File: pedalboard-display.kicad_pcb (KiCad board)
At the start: 2 copper layers, 174 x 111 mm, 206 parts, among them J1 Conn_01x03_Pin, J2 Conn_01x03_Pin, J3 OLED

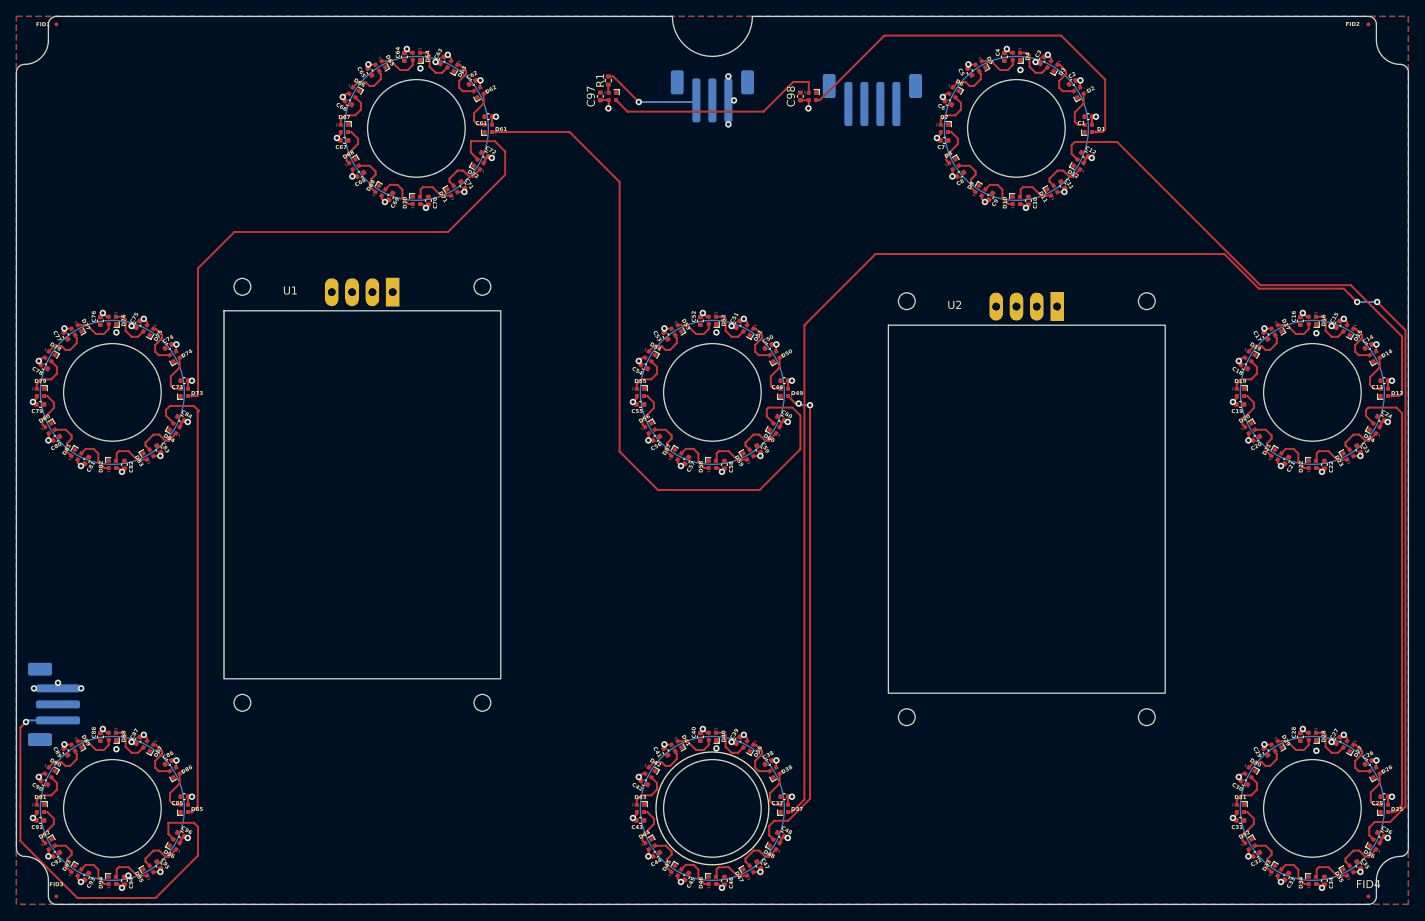
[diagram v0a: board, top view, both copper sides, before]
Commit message: Add 3d models for JST connectors
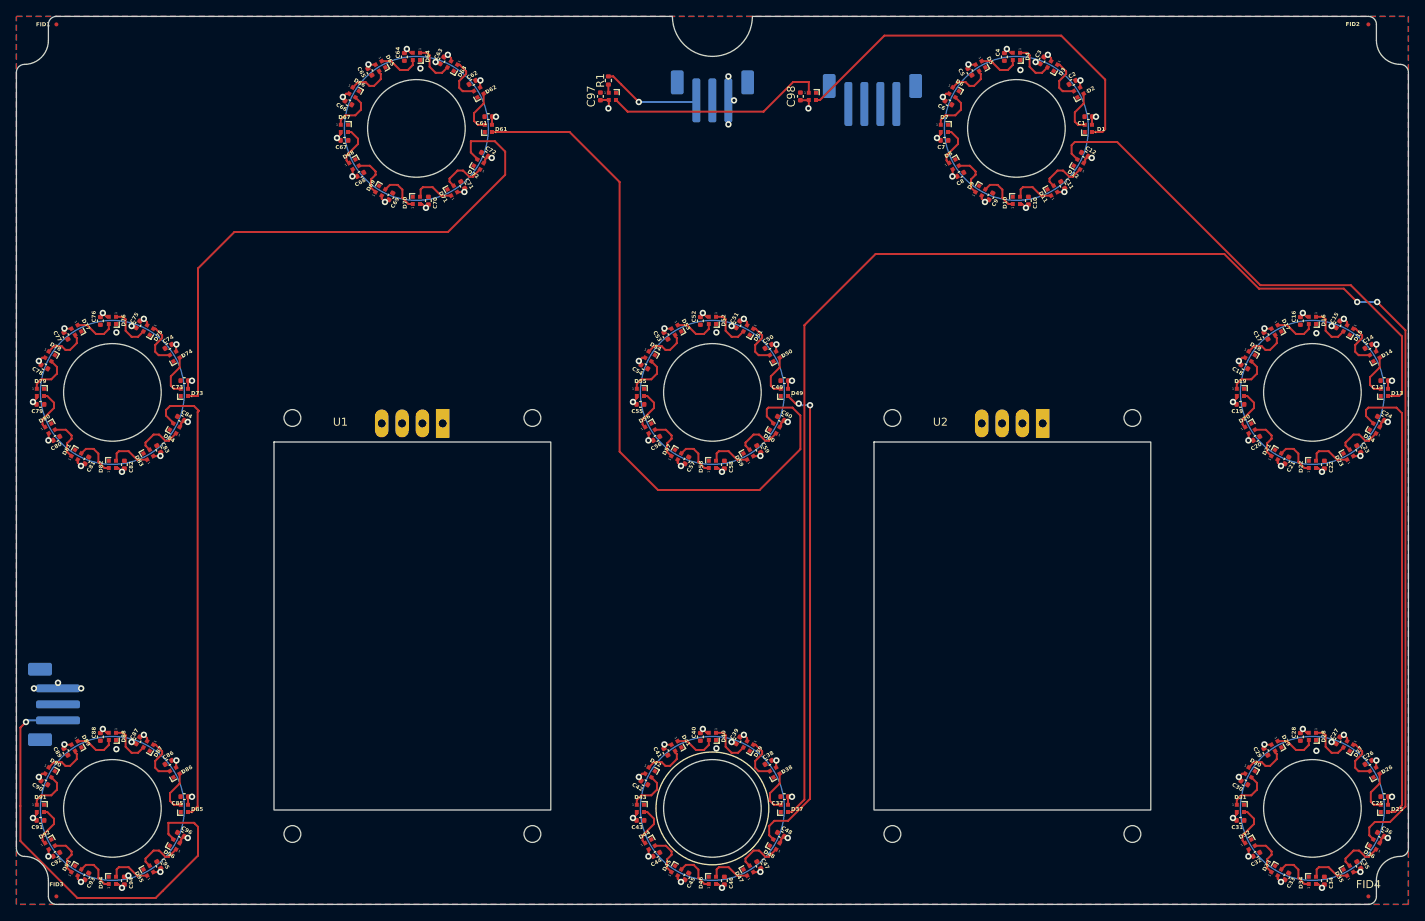
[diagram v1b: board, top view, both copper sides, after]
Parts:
- J1, J2: footprint Connector_JST:JST_PH_B3B-PH-SM4-TB_1x03-1MP_P2.00mm_Vertical -> Library:JST_PH_B3B-PH-SM4-TB_1x03-1MP_P2.00mm_Vertical
- J3: footprint Connector_JST:JST_PH_B4B-PH-SM4-TB_1x04-1MP_P2.00mm_Vertical -> Library:JST_PH_B4B-PH-SM4-TB_1x04-1MP_P2.00mm_Vertical
- moved U1 17.6 mm to (69.5, 101.2)
- moved U2 14.7 mm to (144.5, 101.2)

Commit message: Connect all
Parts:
- moved J3 36.7 mm to (144.0, 68.0)
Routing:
- net /I2C_SDA: track 0.00 -> 127.9 mm, vias 0 -> 1
- net /I2C_SCL: track 0.00 -> 111.8 mm, vias 0 -> 1
- net +3.3V: track 0.00 -> 110.7 mm
- net GND: track 13.3 -> 19.3 mm, vias 23 -> 26

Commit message: Small text improvments
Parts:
- J1: value Conn_01x03_Pin -> LED-IN
- J2: value Conn_01x03_Pin -> LED-OUT
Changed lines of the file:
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@@
 			)
 		)
-		(property "Value" "Conn_01x03_Pin"
+		(property "Value" "LED-OUT"
 			(at 0 -4.45 90)
 			(layer "B.Fab")
@@
 		(sheetname "Root")
 		(sheetfile "pedalboard-display.kicad_sch")
-		(attr smd)
+		(attr smd dnp)
 		(fp_line
 			(start -5.085 4.36)
@@
 		(tags "connector JST PH vertical")
 		(property "Reference" "J1"
-			(at 0 5.45 0)
+			(at -5 -5 0)
 			(layer "B.SilkS")
 			(effects
@@
 			)
 		)
-		(property "Value" "Conn_01x03_Pin"
+		(property "Value" "LED-IN"
 			(at 0 -4.45 0)
 			(layer "B.Fab")
@@
 			(xy 116.937822 72) (xy 106.937822 72)
 		)
-		(height 14.24)
+		(height 13)
 		(gr_text "10 mm"
-			(at 111.937822 56.61 0)
+			(at 111.937822 57.85 0)
 			(layer "Dwgs.User")
 			(effects
@@
 			(xy 106.937822 60) (xy 106.937822 84)
 		)
-		(height 20)
+		(height 14.937822)
 		(gr_text "24 mm"
-			(at 85.787822 72 90)
+			(at 90.85 72 90)
 			(layer "Dwgs.User")
 			(effects
@@
 			(xy 106.937822 65.9) (xy 106.937822 78.1)
 		)
-		(height 17)
+		(height 12.937822)
 		(gr_text "12.2 mm"
-			(at 88.787822 72 90)
+			(at 92.85 72 90)
 			(layer "Dwgs.User")
 			(effects

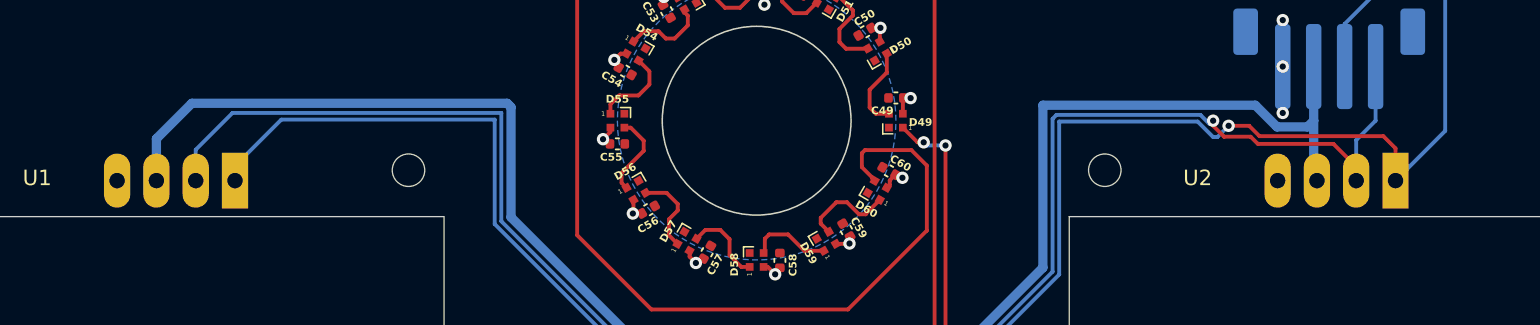
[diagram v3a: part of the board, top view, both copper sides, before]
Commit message: Silkscreen on top
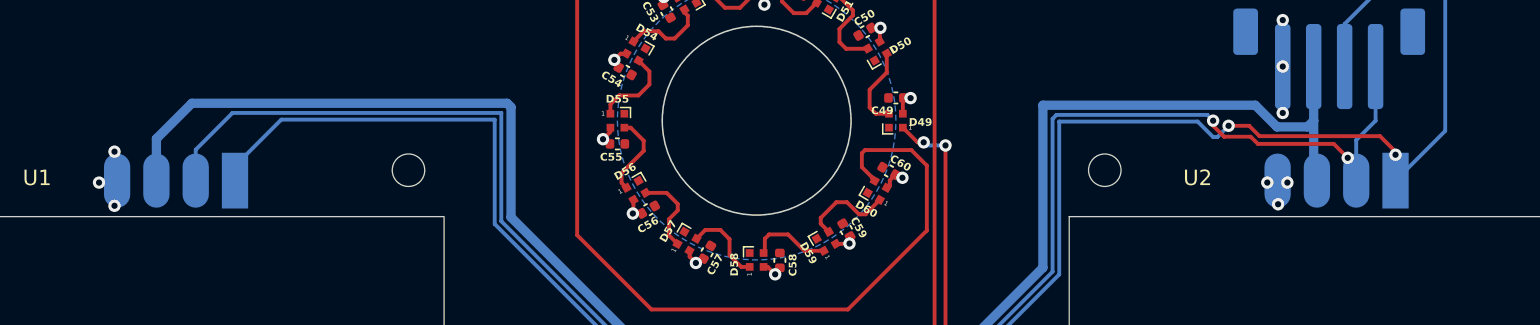
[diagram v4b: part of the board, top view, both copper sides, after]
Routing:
- net GND: track 19.3 -> 26.7 mm, vias 26 -> 32
- net /I2C_SCL: track 111.8 -> 110.0 mm, vias 1 -> 2
- net /I2C_SDA: track 127.9 -> 127.8 mm, vias 1 -> 2
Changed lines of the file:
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@@
 		)
 		(fp_line
-			(start 3.788 -23.9972)
+			(start 4.8 -24)
 			(end 5.118 -23.9972)
 			(stroke
@@
 			(layers "F&B.Cu" "*.Mask")
 		)
-		(pad "1" thru_hole rect
+		(pad "1" smd rect
 			(at 3.788 -25.3272 270)
 			(size 3.6 1.7)
-			(drill 1)
-			(layers "*.Cu" "*.Mask")
-			(remove_unused_layers no)
+			(layers "B.Cu" "B.Paste" "B.Mask")
 			(net 104 "/I2C_SDA")
 			(pinfunction "SDA")
 			(pintype "bidirectional")
 		)
-		(pad "2" thru_hole oval
+		(pad "2" smd oval
 			(at 1.248 -25.3272 270)
 			(size 3.5 1.7)
-			(drill 1)
-			(layers "*.Cu" "*.Mask")
-			(remove_unused_layers no)
+			(layers "B.Cu" "B.Paste" "B.Mask")
 			(net 105 "/I2C_SCL")
 			(pinfunction "SCL")
 			(pintype "input")
 		)
-		(pad "3" thru_hole oval
+		(pad "3" smd oval
 			(at -1.292 -25.3272 270)
 			(size 3.5 1.7)
-			(drill 1)
-			(layers "*.Cu" "*.Mask")
-			(remove_unused_layers no)
+			(layers "B.Cu")
 			(net 103 "+3.3V")
 			(pinfunction "VDD")
 			(pintype "power_in")
 		)
-		(pad "4" thru_hole oval
+		(pad "4" smd oval
 			(at -3.832 -25.3272 270)
 			(size 3.5 1.7)
-			(drill 1)
-			(layers "*.Cu" "*.Mask")
-			(remove_unused_layers no)
+			(layers "B.Cu" "B.Paste" "B.Mask")
 			(net 8 "GND")
 			(pinfunction "VSS")
@@
 		)
 		(fp_line
-			(start 3.788 -23.9972)
+			(start 4.8 -24)
 			(end 5.118 -23.9972)
 			(stroke
@@
 			(layers "F&B.Cu" "*.Mask")
 		)
-		(pad "1" thru_hole rect
+		(pad "1" smd rect
 			(at 3.788 -25.3272 270)
 			(size 3.6 1.7)
-			(drill 1)
-			(layers "*.Cu" "*.Mask")
-			(remove_unused_layers no)
+			(layers "B.Cu" "B.Paste" "B.Mask")
 			(net 104 "/I2C_SDA")
 			(pinfunction "SDA")
 			(pintype "bidirectional")
 		)
-		(pad "2" thru_hole oval
+		(pad "2" smd oval
 			(at 1.248 -25.3272 270)
 			(size 3.5 1.7)
-			(drill 1)
-			(layers "*.Cu" "*.Mask")
-			(remove_unused_layers no)
+			(layers "B.Cu" "B.Paste" "B.Mask")
 			(net 105 "/I2C_SCL")
 			(pinfunction "SCL")
 			(pintype "input")
 		)
-		(pad "3" thru_hole oval
+		(pad "3" smd oval
 			(at -1.292 -25.3272 270)
 			(size 3.5 1.7)
-			(drill 1)
-			(layers "*.Cu" "*.Mask")
-			(remove_unused_layers no)
+			(layers "B.Cu")
 			(net 103 "+3.3V")
 			(pinfunction "VDD")
 			(pintype "power_in")
 		)
-		(pad "4" thru_hole oval
+		(pad "4" smd oval
 			(at -3.832 -25.3272 270)
 			(size 3.5 1.7)
-			(drill 1)
-			(layers "*.Cu" "*.Mask")
-			(remove_unused_layers no)
+			(layers "B.Cu" "B.Paste" "B.Mask")
 			(net 8 "GND")
 			(pinfunction "VSS")
@@
 	)
 	(via
+		(at 65.5 77.5)
+		(size 0.8)
+		(drill 0.4)
+		(layers "F.Cu" "B.Cu")
+		(net 8)
+	)
+	(via
+		(at 140.7 77.4)
+		(size 0.8)
+		(drill 0.4)
+		(layers "F.Cu" "B.Cu")
+		(net 8)
+	)
+	(via
 		(at 32.5 116.6)
 		(size 0.8)
@@
 	)
 	(via
+		(at 140 76)
+		(size 0.8)
+		(drill 0.4)
+		(layers "F.Cu" "B.Cu")
+		(net 8)
+	)
+	(via
 		(at 145.5 31.7)
 		(size 0.8)
@@
 	)
 	(via
+		(at 65.5 74)
+		(size 0.8)
+		(drill 0.4)
+		(layers "F.Cu" "B.Cu")
+		(net 8)
+	)
+	(via
+		(at 64.5 76)
+		(size 0.8)
+		(drill 0.4)
+		(layers "F.Cu" "B.Cu")
+		(net 8)
+	)
+	(via
 		(at 107.5 64.5)
 		(size 0.8)
@@
 	)
 	(via
+		(at 141.3 76)
+		(size 0.8)
+		(drill 0.4)
+		(layers "F.Cu" "B.Cu")
+		(net 8)
+	)
+	(via
 		(at 147.4 30.7)
 		(size 0.8)
@@
 	)
 	(segment
+		(start 65.668 74.168)
+		(end 65.5 74)
+		(width 0.25)
+		(layer "B.Cu")
+		(net 8)
+	)
+	(segment
 		(start 25.2 109)
 		(end 28.1 109)
@@
 	)
 	(segment
+		(start 65.668 75.8728)
+		(end 65.668 74.168)
+		(width 0.25)
+		(layer "B.Cu")
+		(net 8)
+	)
+	(segment
 		(start 141 68.5)
 		(end 141 65.5)
@@
 	)
 	(segment
+		(start 141.3728 75.8728)
+		(end 141.4 75.9)
+		(width 0.25)
+		(layer "B.Cu")
+		(net 8)
+	)
+	(segment
+		(start 65.668 77.332)
+		(end 65.5 77.5)
+		(width 0.25)
+		(layer "B.Cu")
+		(net 8)
+	)
+	(segment
+		(start 64.6272 75.8728)
+		(end 64.5 76)
+		(width 0.25)
+		(layer "B.Cu")
+		(net 8)
+	)
+	(segment
 		(start 25.2 109)
 		(end 22.2 109)
@@
 	)
 	(segment
+		(start 65.668 75.8728)
+		(end 65.668 77.332)
+		(width 0.25)
+		(layer "B.Cu")
+		(net 8)
+	)
+	(segment
 		(start 141 68.5)
 		(end 141 71.5)
@@
 	)
 	(segment
+		(start 140.668 75.8728)
+		(end 141.3728 75.8728)
+		(width 0.25)
+		(layer "B.Cu")
+		(net 8)
+	)
+	(segment
+		(start 65.668 75.8728)
+		(end 64.6272 75.8728)
+		(width 0.25)
+		(layer "B.Cu")
+		(net 8)
+	)
+	(segment
 		(start 109 35.5)
 		(end 109.7 35.5)
@@
 	)
 	(segment
+		(start 140.668 75.8728)
+		(end 140.668 77.668)
+		(width 0.25)
+		(layer "B.Cu")
+		(net 8)
+	)
+	(segment
 		(start 136.27 42.38)
 		(end 136.27 43.014229)
@@
 	)
 	(segment
-		(start 137.5 72.33)
-		(end 138.83 72.33)
+		(start 148.288 74)
+		(end 147.288 73)
 		(width 0.25)
 		(layer "F.Cu")
@@
 	(segment
 		(start 138.83 72.33)
-		(end 139.5 73)
+		(end 137.5 72.33)
 		(width 0.25)
 		(layer "F.Cu")
@@
 	)
 	(segment
-		(start 148.288 73.788)
-		(end 148.288 75.8728)
+		(start 139.5 73)
+		(end 138.83 72.33)
 		(width 0.25)
 		(layer "F.Cu")
@@
 	)
 	(segment
-		(start 147.5 73)
-		(end 148.288 73.788)
+		(start 147.288 73)
+		(end 139.5 73)
 		(width 0.25)
 		(layer "F.Cu")
 		(net 104)
 	)
-	(segment
-		(start 139.5 73)
-		(end 147.5 73)
-		(width 0.25)
-		(layer "F.Cu")
+	(via
+		(at 137.5 72.33)
+		(size 0.8)
+		(drill 0.4)
+		(layers "F.Cu" "B.Cu")
 		(net 104)
 	)
 	(via
-		(at 137.5 72.33)
+		(at 148.288 74.2)
 		(size 0.8)
 		(drill 0.4)
@@
 	)
 	(segment
-		(start 151.5 72.6608)
+		(start 148.288 74)
 		(end 148.288 75.8728)
 		(width 0.25)
@@
 	)
 	(segment
+		(start 148.288 75.8728)
+		(end 151.5 72.6608)
+		(width 0.25)
+		(layer "B.Cu")
+		(net 104)
+	)
+	(segment
 		(start 90.07 71.93)
 		(end 76.2808 71.93)
@@
 	(segment
 		(start 144.2752 73.5)
-		(end 145.748 74.9728)
+		(end 144.3 73.5)
 		(width 0.25)
 		(layer "F.Cu")
@@
 	)
 	(segment
-		(start 145.748 74.9728)
-		(end 145.748 75.8728)
+		(start 136.5 72.327021)
+		(end 137.207979 73.035)
 		(width 0.25)
 		(layer "F.Cu")
@@
 	)
 	(segment
-		(start 136.5 72.327021)
-		(end 137.207979 73.035)
+		(start 144.3 73.5)
+		(end 145.2 74.4)
 		(width 0.25)
 		(layer "F.Cu")
@@
 		(net 105)
 	)
+	(via
+		(at 145.2 74.4)
+		(size 0.8)
+		(drill 0.4)
+		(layers "F.Cu" "B.Cu")
+		(net 105)
+	)
+	(segment
+		(start 100.125 88.125)
+		(end 119.758884 88.125)
+		(width 0.25)
+		(layer "B.Cu")
+		(net 105)
+	)
 	(segment
-		(start 135.678112 71.625)
-		(end 136.276556 72.223444)
+		(start 126.125 71.876888)
+		(end 126.376888 71.625)
+		(width 0.25)
+		(layer "B.Cu")
+		(net 105)
+	)
+	(segment
+		(start 70.748 73.877)
+		(end 73.125 71.5)
 		(width 0.25)
 		(layer "B.Cu")
@@
 	)
 	(segment
-		(start 145.748 73.252)
-		(end 145.748 75.8728)
+		(start 136.125 71.625)
+		(end 136.276556 71.776556)
 		(width 0.25)
 		(layer "B.Cu")
@@
 	)
 	(segment
-		(start 100.125 88.125)
-		(end 119.758884 88.125)
+		(start 126.376888 71.625)
+		(end 136.125 71.625)
 		(width 0.25)
 		(layer "B.Cu")
@@
 	)
 	(segment
-		(start 70.748 73.877)
-		(end 73.125 71.5)
+		(start 70.748 75.8728)
+		(end 70.748 73.877)
 		(width 0.25)
 		(layer "B.Cu")
@@
 	)
 	(segment
-		(start 70.748 75.8728)
-		(end 70.748 73.877)
+		(start 145.748 73.252)
+		(end 145.748 75.8728)
 		(width 0.25)
 		(layer "B.Cu")
@@
 		(width 0.25)
 		(layer "B.Cu")
-		(net 105)
-	)
-	(segment
-		(start 126.376888 71.625)
-		(end 135.678112 71.625)
-		(width 0.25)
-		(layer "B.Cu")
-		(net 105)
-	)
-	(segment
-		(start 126.125 71.876888)
-		(end 126.376888 71.625)
-		(width 0.25)
-		(layer "B.Cu")
